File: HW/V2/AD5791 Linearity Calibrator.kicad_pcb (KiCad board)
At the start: 4 copper layers, 80 x 100 mm, 60 parts, among them J2 VREFP, J3 VREFN, J5 VREFP, J7 PWR, SW1 RST, U10 ADR1399, U11 L79L15, U12 7533, U13 ADuM1400xRW, U4 L78L15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

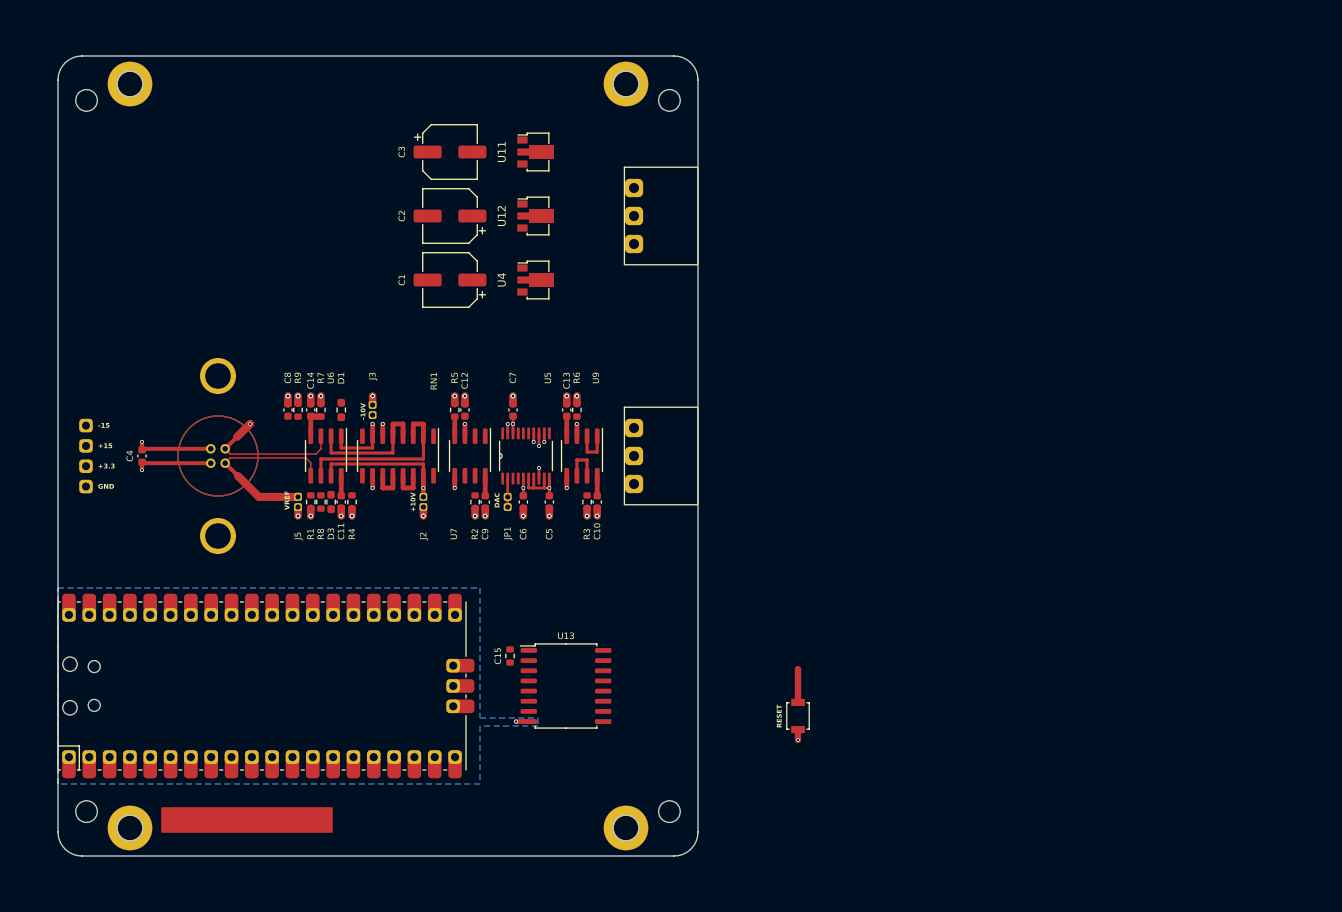
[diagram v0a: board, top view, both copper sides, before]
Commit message: updated layout
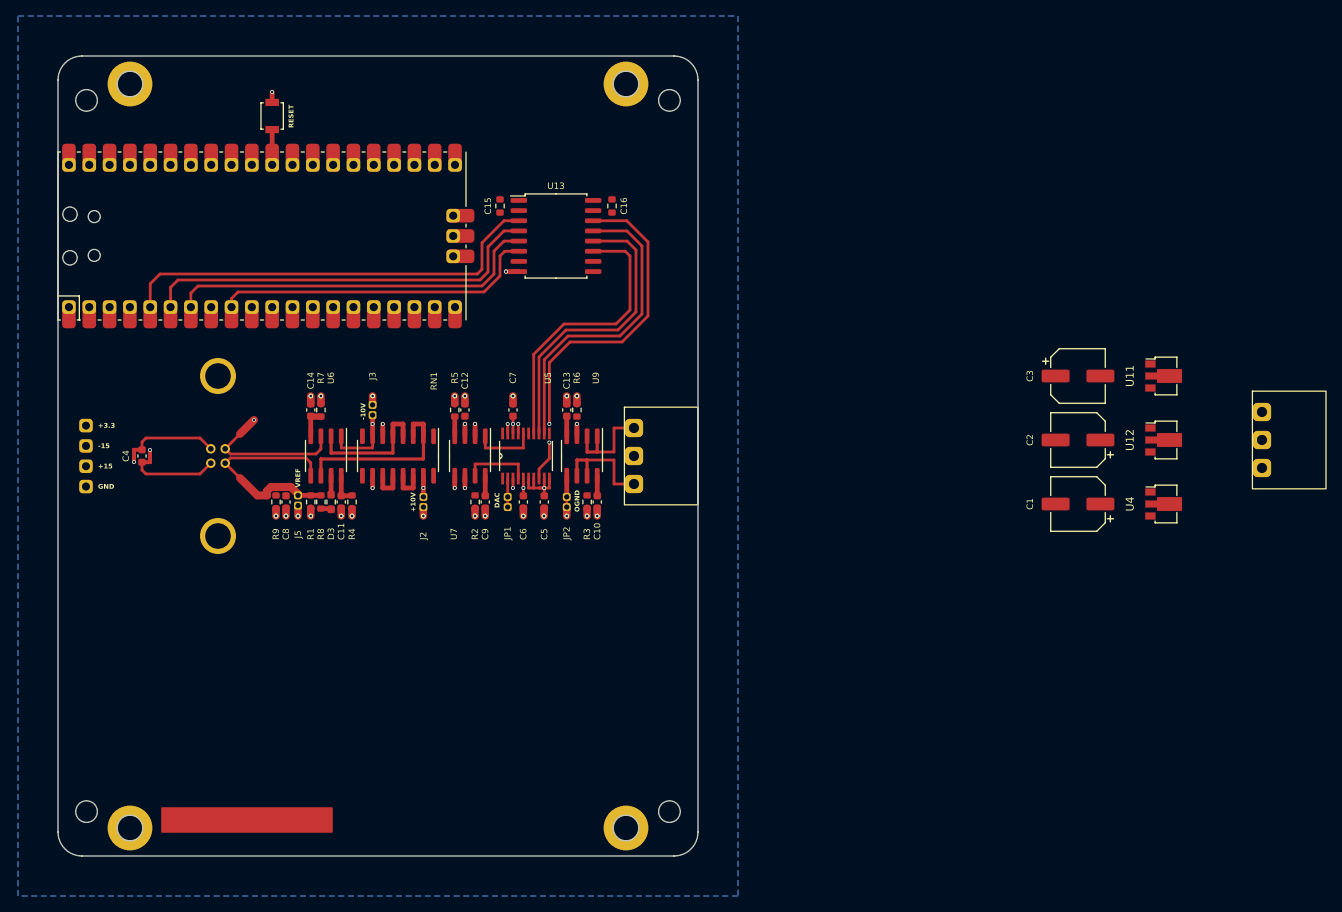
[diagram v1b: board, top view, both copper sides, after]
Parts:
- removed D1: 5819, Resistor_SMD:R_0603_1608Metric_Pad0.98x0.95mm_HandSolder
- added C16: 10uF, Resistor_SMD:R_0603_1608Metric, F.Cu at (139.2, 68.8)
- added JP2: GND, Connector_PinHeader_1.27mm:PinHeader_1x02_P1.27mm_Vertical, F.Cu at (133.6, 105.1)
- moved REF** 127.8 mm to (236.5, 129.0)
- moved SW1 99.7 mm to (96.8, 57.5), turned to -90 degrees
- moved C1 83.3 mm to (197.5, 106.0)
- moved C2 83.3 mm to (197.5, 98.0)
- moved C3 83.3 mm to (197.5, 90.0)
- moved J1 83.3 mm to (228.5, 98.0)
- moved U11 83.3 mm to (208.5, 90.0)
- moved U12 83.3 mm to (208.5, 98.0)
- moved U4 83.3 mm to (208.5, 106.0)
- moved C15 56.3 mm to (125.2, 68.8)
- moved U13 56.3 mm to (132.2, 72.5)
- moved U8 56.2 mm to (95.5, 72.5)
- moved R9 11.8 mm to (97.2, 105.8), turned to 90 degrees
- moved C8 11.5 mm to (98.5, 105.8), turned to -90 degrees
- moved C5 0.63 mm to (130.8, 105.8)
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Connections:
- J7 pad 1: -15V -> +3.3V
- J7 pad 2: +15V -> -15V
- J7 pad 3: +3.3V -> +15V
- U13 pad 11: /SDIN -> /ISO ~{SYNC}
- U13 pad 12: /SCLK -> /ISO SCLK
- U13 pad 13: /~{SYNC} -> /ISO SDIN
- U13 pad 14: /~{LDAC} -> /ISO ~{LDAC}
- U13 pad 15: Net-(U13-GND2-Pad15) -> GND
- U13 pad 16: unconnected-(U13-VDD2-Pad16) -> +3.3V
- U13 pad 3: unconnected-(U13-VIA-Pad3) -> /~{LDAC}
- U13 pad 4: unconnected-(U13-VIB-Pad4) -> /SDIN
- U13 pad 5: unconnected-(U13-VIC-Pad5) -> /SCLK
- U13 pad 6: unconnected-(U13-VID-Pad6) -> /~{SYNC}
- U13 pad 9: Net-(U13-GND2-Pad15) -> GND
- U5 pad 12: /SDIN -> /ISO SDIN
- U5 pad 13: /SCLK -> /ISO SCLK
- U5 pad 14: /~{SYNC} -> /ISO ~{SYNC}
- U5 pad 8: /~{LDAC} -> /ISO ~{LDAC}
- U6 pad 1: Net-(D1-K) -> /-10.5V
- U8 pad 5: unconnected-(U8-GPIO3-Pad5) -> /~{LDAC}
- U8 pad 6: unconnected-(U8-GPIO4-Pad6) -> /SDIN
- U8 pad 7: unconnected-(U8-GPIO5-Pad7) -> /SCLK
- U8 pad 9: unconnected-(U8-GPIO6-Pad9) -> /~{SYNC}
- U9 pad 1: Net-(J4-Pin_3) -> Net-(J4-Pin_1)
- U9 pad 2: Net-(J4-Pin_3) -> Net-(J4-Pin_1)
- U9 pad 6: Net-(J4-Pin_1) -> Net-(J4-Pin_3)
- U9 pad 7: Net-(J4-Pin_1) -> Net-(J4-Pin_3)
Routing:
- net /~{LDAC}: track 1.32 -> 54.2 mm, vias 1 -> 0
- net /SDIN: track 1.07 -> 50.8 mm, vias 1 -> 0
- net /ISO ~{LDAC}: track 0.00 -> 46.7 mm, vias 0 -> 2
- net /SCLK: track 1.57 -> 47.1 mm, vias 1 -> 0
- net /~{SYNC}: track 1.07 -> 40.9 mm, vias 1 -> 0
- net /ISO SDIN: track 0.00 -> 39.2 mm
- net /ISO SCLK: track 0.00 -> 37.6 mm
- net /ISO ~{SYNC}: track 0.00 -> 35.8 mm
- net /+10.5V: track 18.8 -> 5.59 mm
- net /VREFNS: track 0.00 -> 9.61 mm, vias 0 -> 2
- net Net-(RN1F-R6.1): track 12.3 -> 3.05 mm
- net Net-(J4-Pin_3): track 5.22 -> 14.1 mm
- net GND: track 81.0 -> 89.7 mm
- net /VREFPS: track 0.00 -> 8.72 mm, vias 0 -> 2
- net /VREFPF: track 0.00 -> 8.69 mm
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- added copper zone on In2.Cu, net +15V
- added copper zone on In2.Cu, net -15V
- added copper zone on B.Cu, net GND
- added copper zone on In1.Cu, net GND
- removed copper zone on B.Cu, net (none)
- removed copper zone on F.Cu, net (none)
- removed copper zone on In1.Cu, net (none)
- removed copper zone on In2.Cu, net (none)
- removed copper zone on B.Cu, net GNDD
- removed copper zone on In1.Cu, net GNDD
- removed copper zone on In2.Cu, net GNDD
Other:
- board text added: "OGND"

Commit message: updated layout
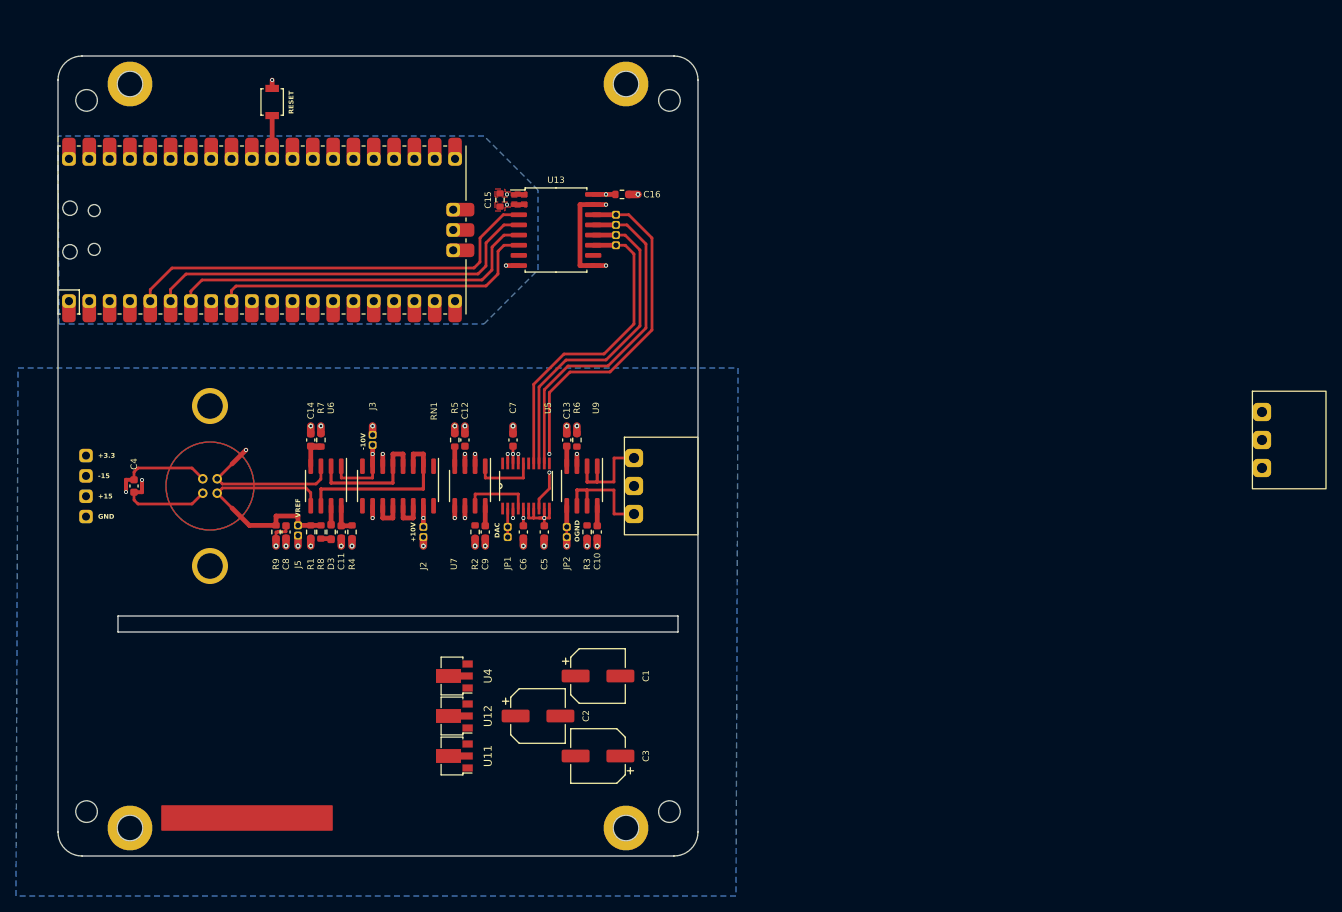
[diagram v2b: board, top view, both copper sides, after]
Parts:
- added J6: SIG, Connector_PinHeader_1.27mm:PinHeader_1x04_P1.27mm_Vertical, F.Cu at (139.8, 69.8)
- moved REF** 139.8 mm to (109.0, 71.8)
- moved U11 101.1 mm to (119.2, 137.5), turned to 180 degrees
- moved U12 95.7 mm to (119.2, 132.5), turned to 180 degrees
- moved U4 91.8 mm to (119.2, 127.5), turned to 180 degrees
- moved C3 76.5 mm to (137.5, 137.5), turned to 180 degrees
- moved C2 75.8 mm to (130.0, 132.5), turned to 0 degrees
- moved C1 63.7 mm to (137.5, 127.5), turned to 0 degrees
- moved C4 3.88 mm to (79.5, 103.8)
- moved H1 3.88 mm to (89.0, 93.8)
- moved H2 3.88 mm to (89.0, 113.8)
- moved U10 3.88 mm to (89.9, 104.6)
- moved C10 3.75 mm to (137.4, 109.5)
- moved C11 3.75 mm to (105.4, 109.5)
- moved C12 3.75 mm to (120.9, 98.0)
- moved C13 3.75 mm to (133.6, 98.0)
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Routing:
- net GND: track 89.7 -> 106.0 mm, vias 16 -> 19
- net /ISO ~{LDAC}: track 46.7 -> 53.7 mm
- net /ISO ~{SYNC}: track 35.8 -> 42.7 mm
- net /ISO SDIN: track 39.2 -> 46.1 mm
- net /ISO SCLK: track 37.6 -> 44.3 mm
- net Net-(C8-Pad1): track 0.00 -> 3.76 mm, vias 0 -> 1
- net +3.3V: track 8.96 -> 11.7 mm, vias 1 -> 2
- net /7VREF: track 28.7 -> 30.8 mm, vias 1 -> 0
- net /~{LDAC}: track 54.2 -> 53.1 mm
- net Net-(SW1-B): track 4.41 -> 5.41 mm
- net /SDIN: track 50.8 -> 50.0 mm
- net GNDD: track 2.90 -> 2.65 mm, vias 2 -> 3
- net +3.3VP: vias 0 -> 1
- added copper zone on B.Cu, net (none)
- added copper zone on F.Cu, net (none)
- added copper zone on In1.Cu, net (none)
- added copper zone on In2.Cu, net (none)
- added copper zone on In2.Cu, net +3.3V
- added copper zone on F.Cu, net +3.3VP
- added copper zone on B.Cu, net GNDD
- added copper zone on F.Cu, net GNDD
- added copper zone on In1.Cu, net GNDD
- added copper zone on In2.Cu, net GNDD
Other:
- outline, holes or cut-outs redrawn

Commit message: updated files
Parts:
- removed H1, H2: MountingHole_Pad, MountingHole:MountingHole_3.2mm_M3_DIN965_Pad
- added J8: VREFN, Connector_PinHeader_1.27mm:PinHeader_1x02_P1.27mm_Vertical, F.Cu at (89.0, 103.8)
- moved J1 85.0 mm to (150.0, 130.5)
- moved U4 35.0 mm to (84.2, 127.8), turned to -90 degrees
- moved U11 24.8 mm to (94.5, 136.0), turned to -90 degrees
- moved C3 16.2 mm to (130.2, 123.0)
- moved U12 14.3 mm to (105.0, 133.5), turned to -90 degrees
- moved C1 12.8 mm to (130.2, 138.0)
- moved C2 2.02 mm to (130.2, 130.5)
- moved C15 0.86 mm to (124.8, 67.3), turned to 0 degrees
- moved C16 0.75 mm to (141.2, 67.3)
- moved J6 0.75 mm to (140.5, 69.8)
- moved U13 0.75 mm to (133.0, 71.8)
- moved C4 0.62 mm to (78.9, 103.8)
- moved SW1 0.50 mm to (96.8, 56.2)
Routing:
- net +3.3VP: track 0.00 -> 50.4 mm
- net GNDD: track 2.65 -> 5.42 mm, vias 3 -> 4
- net /~{SYNC}: track 41.2 -> 42.0 mm
- net /~{LDAC}: track 53.1 -> 53.9 mm
- net /SCLK: track 46.8 -> 47.6 mm
- net /ISO ~{SYNC}: track 42.7 -> 43.5 mm
- net /ISO ~{LDAC}: track 53.7 -> 54.5 mm
- net /ISO SDIN: track 46.1 -> 46.8 mm
- net /ISO SCLK: track 44.3 -> 45.1 mm
- net /SDIN: track 50.0 -> 50.8 mm
- net -15V: track 18.1 -> 18.7 mm
- net +15V: track 21.2 -> 21.8 mm
- net Net-(SW1-B): track 5.41 -> 4.91 mm
- removed copper zone on F.Cu, net +3.3VP
- removed copper zone on F.Cu, net GNDD
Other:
- outline, holes or cut-outs redrawn

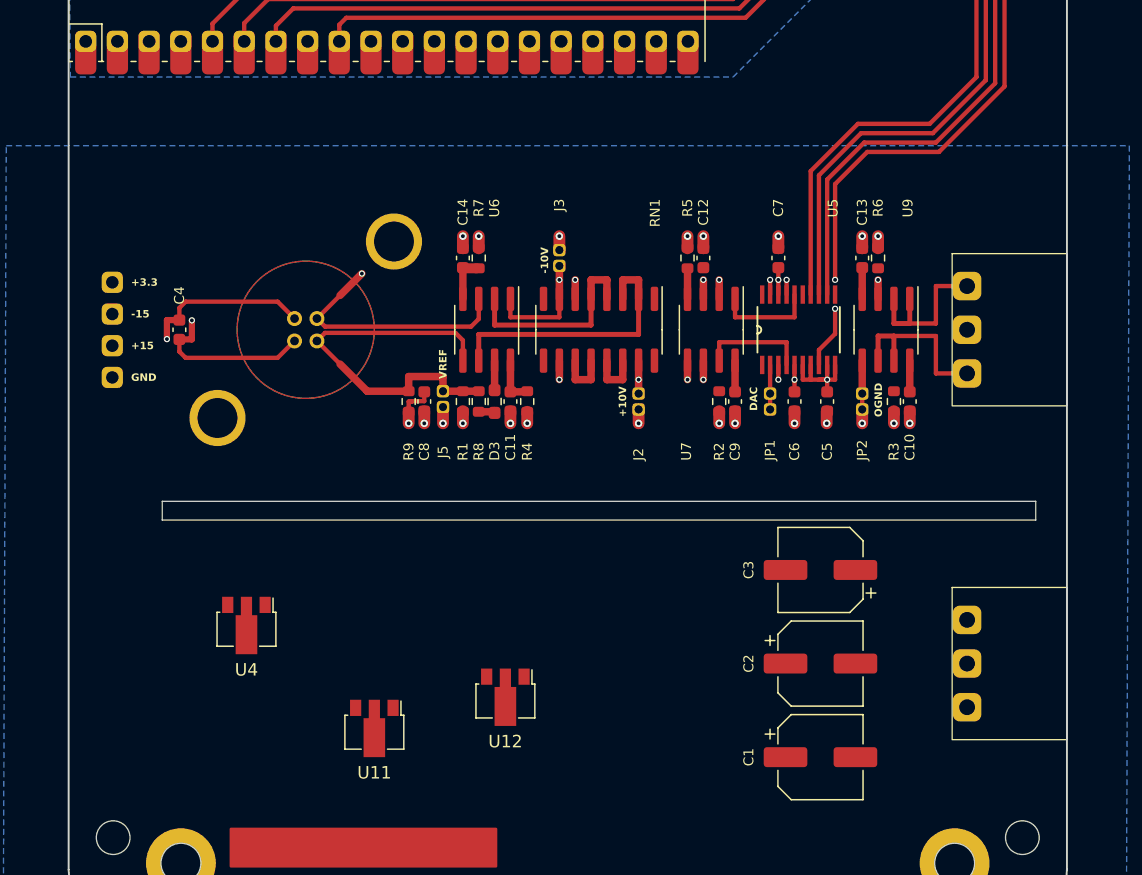
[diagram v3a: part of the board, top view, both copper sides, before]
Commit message: updated layout
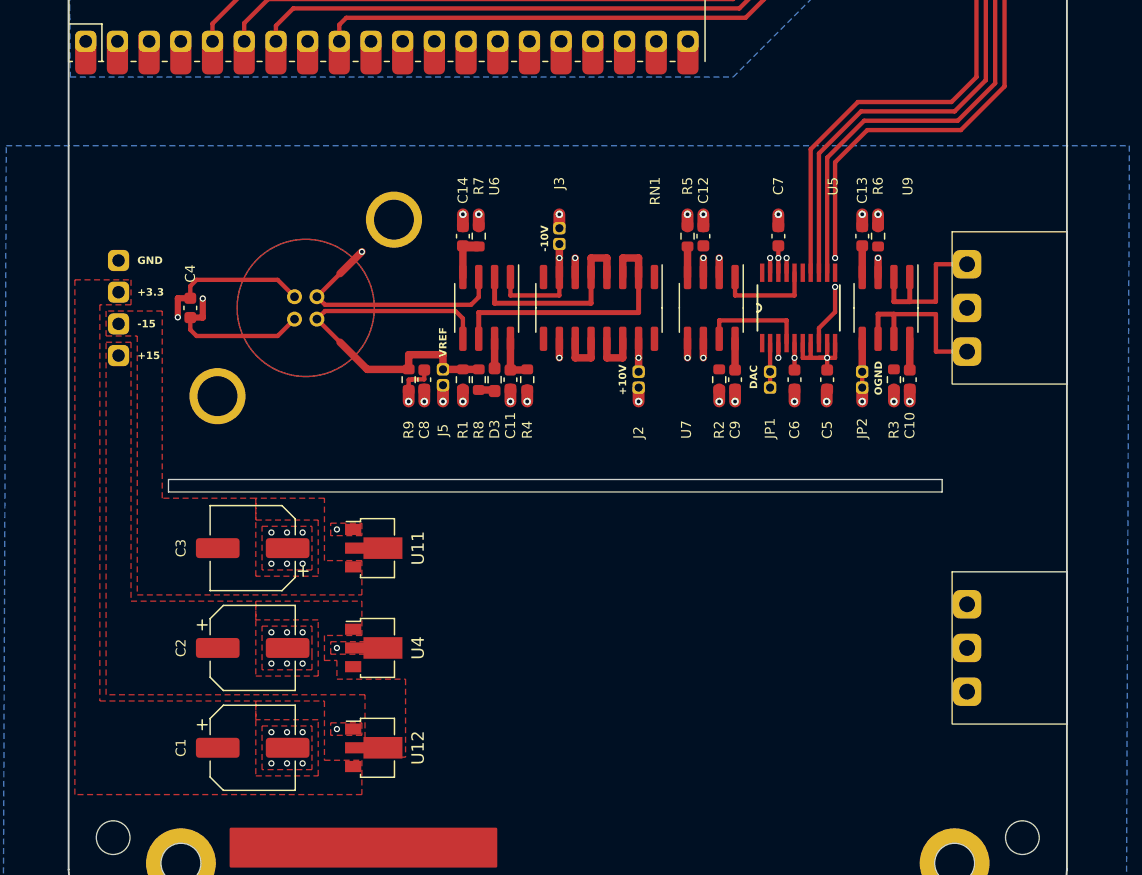
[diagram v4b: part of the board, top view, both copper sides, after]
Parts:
- moved C3 45.5 mm to (84.8, 121.2)
- moved C2 45.5 mm to (84.8, 129.2)
- moved C1 45.5 mm to (84.8, 137.2)
- moved U11 14.8 mm to (94.8, 121.2), turned to 0 degrees
- moved U12 10.9 mm to (94.8, 137.2), turned to 0 degrees
- moved U4 10.6 mm to (94.8, 129.2), turned to 0 degrees
- moved C4 1.96 mm to (79.8, 102.0)
- moved J7 1.82 mm to (74.0, 98.2)
- moved C10 1.75 mm to (137.4, 107.8)
- moved C11 1.75 mm to (105.4, 107.8)
- moved C12 1.75 mm to (120.9, 96.2)
- moved C13 1.75 mm to (133.6, 96.2)
- moved C14 1.75 mm to (101.6, 96.2)
- moved C5 1.75 mm to (130.8, 107.8)
- moved C6 1.75 mm to (128.2, 107.8)
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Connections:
- J7 pad 1: +3.3V -> GND
- J7 pad 2: -15V -> +3.3V
- J7 pad 3: +15V -> -15V
- J7 pad 4: GND -> +15V
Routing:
- net -15V: track 18.7 -> 17.9 mm
- net +15V: track 21.8 -> 20.9 mm
- net /ISO SDIN: track 46.8 -> 46.1 mm
- net /ISO ~{SYNC}: track 43.5 -> 42.7 mm
- net /ISO ~{LDAC}: track 54.5 -> 53.8 mm
- net /ISO SCLK: track 45.1 -> 44.3 mm
- net GND: vias 19 -> 40
- added copper zone on F.Cu, net +15V
- added copper zone on F.Cu, net +3.3V
- added copper zone on F.Cu, net -15V
- added copper zone on F.Cu, net GND
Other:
- outline, holes or cut-outs redrawn

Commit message: Finished V2 layout (rev1)
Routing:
- net /+10.5V: track 5.59 -> 23.2 mm
- net GNDD: track 5.42 -> 19.1 mm
- net /BUFIN: track 9.62 -> 21.3 mm
- net /-10.5V: track 11.0 -> 22.7 mm
- net Net-(RN1F-R6.1): track 3.05 -> 11.5 mm
- net Net-(RN1B-R2.1): track 24.4 -> 21.0 mm
- net Net-(J4-Pin_1): track 12.8 -> 14.7 mm
- net Net-(U9C-V-): track 2.63 -> 3.93 mm
- net Net-(U9C-V+): track 2.63 -> 3.93 mm
- net Net-(U7C-V-): track 2.58 -> 3.88 mm
- net Net-(U7C-V+): track 2.63 -> 3.93 mm
- net GND: track 106.0 -> 106.9 mm, vias 40 -> 41
- net Net-(RN1D-R4.1): track 16.2 -> 15.4 mm
- net /ISO ~{LDAC}: track 53.8 -> 53.2 mm
- net Net-(J4-Pin_3): track 14.1 -> 14.6 mm
- added copper zone on F.Cu, net Net-(J1-Pin_1)
- added copper zone on F.Cu, net Net-(J1-Pin_3)
